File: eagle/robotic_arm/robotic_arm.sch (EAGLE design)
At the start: 104 parts, among them J2 (ID,OD)=(2.1,5.5)MM, SW1 5A/28V, Y1 16MHz

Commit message: Fucked up.  Forgot pull down and current limiting resistors on PWM driver to servosgit add -A  Added them.  Need to increase size of board and reroute
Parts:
- added R10, R12, R14, R4, R6, R8: 10KΩ, MrSwirlyEyes:RESISTORSMD-0805_1/8W_10K_5%
- added R11, R13, R15, R5, R7, R9: 100Ω, MrSwirlyEyes:RESISTORSMD-0805_1/8W_100_5%
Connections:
- new net N$1: R11.1, SERVO_WRIST.SIG
- new net N$4: R9.1, SERVO_THUMB.SIG
- new net N$6: R7.1, SERVO_INDEX.SIG
- new net N$7: R5.1, SERVO_MIDDLE.SIG
- new net N$8: R15.1, SERVO_RING.SIG
- new net N$9: R13.1, SERVO_PINKY.SIG
- net GND: now also R10.1, R12.1, R14.1, R4.1, R6.1, R8.1
- net SERVO_INDEX: now also R6.2, R7.2; no longer SERVO_MIDDLE.SIG
- net SERVO_MIDDLE: now also R4.2, R5.2; no longer SERVO_INDEX.SIG
- net SERVO_PINKY: now also R12.2, R13.2; no longer SERVO_WRIST.SIG
- net SERVO_RING: now also R14.2, R15.2; no longer SERVO_THUMB.SIG
- net SERVO_THUMB: now also R8.2, R9.2; no longer SERVO_RING.SIG
- net SERVO_WRIST: now also R10.2, R11.2; no longer SERVO_PINKY.SIG
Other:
- note removed: "WIRE DEMUX"
- moved on the sheet: C1, C10, C11, C12, C13, C14, C15, C16, C17, C2, C8, C9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

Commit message: Robotic Arm, Rev 1:  Completed all routes.  Messy as shit.  Much clean up to do
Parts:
- A6: value ANTENNASMD5 -> 2.4GHz/802.11/0.5dBi/3W
- B1: value 748421245 -> Impedence UNBAL/BAL (50Ω/100Ω)
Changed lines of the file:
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@@
 <setting verticaltext="up"/>
 </settings>
-<grid distance="0.1" unitdist="inch" unit="inch" style="lines" multiple="1" display="yes" altdistance="0.05" altunitdist="inch" altunit="inch"/>
+<grid distance="0.1" unitdist="inch" unit="inch" style="lines" multiple="1" display="no" altdistance="0.01" altunitdist="inch" altunit="inch"/>
 <layers>
 <layer number="1" name="Top" color="4" fill="1" visible="no" active="no"/>
@@
 <part name="R42" library="MrSwirlyEyes" deviceset="RESISTOR" device="SMD-0805_1/8W_10K_5%" value="10KΩ"/>
 <part name="C51" library="MrSwirlyEyes" deviceset="CAP_CERAMIC" device="_SMD-805_0.1UF-50V-10%" value="0.1uF/50V"/>
-<part name="MCU" library="MrSwirlyEyes" deviceset="ATMEGA128RFA1" device=""/>
+<part name="MCU" library="MrSwirlyEyes" deviceset="ATMEGA128RFA1" device="" value="ATMEGA128RFA1"/>
 <part name="C52" library="MrSwirlyEyes" deviceset="CAP_CERAMIC" device="_SMD-805_0.1UF-50V-10%" value="0.1uF/50V"/>
 <part name="C53" library="MrSwirlyEyes" deviceset="CAP_CERAMIC" device="_SMD-805-1UF-25V-10%" value="1uF/25V"/>
@@
 <part name="GND96" library="MrSwirlyEyes" deviceset="GND" device=""/>
 <part name="GND97" library="MrSwirlyEyes" deviceset="AGND" device=""/>
-<part name="B1" library="lib_kenmei" deviceset="BALUN" device="0805" value="748421245"/>
+<part name="B1" library="lib_kenmei" deviceset="BALUN" device="0805" value="Impedence UNBAL/BAL (50Ω/100Ω)"/>
 <part name="C61" library="MrSwirlyEyes" deviceset="CAP_CERAMIC" device="_SMD-805_22PF-250V-5%" value="22PF/250V"/>
 <part name="GND98" library="MrSwirlyEyes" deviceset="GND" device=""/>
 <part name="C62" library="MrSwirlyEyes" deviceset="CAP_CERAMIC" device="_SMD-805-0.75PF-100V-33%" value="0.75PF/100V"/>
 <part name="GND99" library="MrSwirlyEyes" deviceset="GND" device=""/>
-<part name="A6" library="lib_kenmei" deviceset="ANTENNA" device="SMD5"/>
+<part name="A6" library="lib_kenmei" deviceset="ANTENNA" device="SMD5" value="2.4GHz/802.11/0.5dBi/3W"/>
 <part name="R43" library="MrSwirlyEyes" deviceset="RESISTOR" device="SMD-0805_1/8W_10K_5%" value="10KΩ"/>
 <part name="SUPPLY71" library="MrSwirlyEyes" deviceset="VCC" device=""/>

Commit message: Rev 1: Board complete.  Sent to Fab
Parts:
- removed C56: 0.1uF/50V, MrSwirlyEyes:CAP_CERAMIC_SMD-805_0.1UF-50V-10%
- removed C84: 100UF/16V, MrSwirlyEyes:CAP_POLARIZED_ALUM-ELECTROLYTIC_SMD_100UF-16V-20%
- removed J2: (ID,OD)=(2.1,5.5)MM, MrSwirlyEyes:POWER_JACK-BARREL_ID2.1MM-OD5.5MM
- removed SUPPLY51, SUPPLY52: 2PT_GND_TIE, SparkFun-PowerSymbols:2PT_GND_TIE
- added ANALOG_BR, NOISE_BR: 2PT_GND_TIE, PiB_power_symbols:2PT_GND_TIE
- added C21, C23, C24: 1uF/25V, PiB_capacitors:1UF_SMD-805_25V-10%
- added C22: 0.1uF/50V, PiB_capacitors:0.1UF_SMD-805_50V-10%
- added J1: (ID,OD)=(2.1,5.5)MM, PiB_connectors:POWER_JACK-BARREL_ID2.1MM-OD5.5MM
- A6: device lib_kenmei:ANTENNASMD5 -> PiB_radio_frequency:ANTENNA_SMD-CHIP_2.4GHZ-0.5DBI-3W
- AVR_ISP: device MrSwirlyEyes:AVR_SPI_PRG_6NS -> PiB_connectors:AVR_SPI_PRG_6NS
- B1: device lib_kenmei:BALUN0805 -> PiB_radio_frequency:BALUN_SMD-0805_UNBAL/BAL-50/100
- BATT1: device MrSwirlyEyes:BATTERYPTH_HOLES -> PiB:BATTERYPTH_HOLES
- C1, C10, C12, C14, C16, C19, C26, C3, C4, C47, C48, C49, C5, C50, C51, C52, C54, C6, C63, C7, C79, C8, C81, C83, C93, C96, C98: device MrSwirlyEyes:CAP_CERAMIC_SMD-805_0.1UF-50V-10% -> PiB_capacitors:0.1UF_SMD-805_50V-10%
- C11, C13, C15, C17, C2, C9: value 100UF/16V -> 10uF/20V; device MrSwirlyEyes:CAP_POLARIZED_ALUM-ELECTROLYTIC_SMD_100UF-16V-20% -> PiB_capacitors:10UF-POLARIZED_SMD-1206_20V-20%
- C18, C25, C82, C92, C94, C95, C97: device MrSwirlyEyes:CAP_CERAMIC_SMD-805_10UF-25V-10% -> PiB_capacitors:10UF_CER_SMD-805_25V-10%
- C20: value 220uF/16V -> 100UF/16V; device MrSwirlyEyes:CAP_POLARIZED_ALUM-ELECTROLYTIC_SMD_220UF-16V-20% -> PiB_capacitors:100UF-POLARIZED_SMD_16V-20%
- C53, C55, C57, C58: device MrSwirlyEyes:CAP_CERAMIC_SMD-805-1UF-25V-10% -> PiB_capacitors:1UF_SMD-805_25V-10%
- C59, C60: device MrSwirlyEyes:CAP_CERAMIC_SMD-805_12PF-250V-5% -> PiB_capacitors:12PF_SMD-805_250V-5%
- C61: device MrSwirlyEyes:CAP_CERAMIC_SMD-805_22PF-250V-5% -> PiB_capacitors:22PF_SMD-805_250V-5%
- C62: device MrSwirlyEyes:CAP_CERAMIC_SMD-805-0.75PF-100V-33% -> PiB_capacitors:0.75PF_SMD-805_100V-33%
- C80: device MrSwirlyEyes:CAP_POLARIZED_ALUM-ELECTROLYTIC_SMD_220UF-16V-20% -> PiB_capacitors:220UF-POLARIZED_SMD_16V-20%
- C85: value 1uF/25V -> 0.1uF/50V; device MrSwirlyEyes:CAP_CERAMIC_SMD-805-1UF-25V-10% -> PiB_capacitors:0.1UF_SMD-805_50V-10%
- D1, D6, D7: device MrSwirlyEyes:DIODE_GEN-PURPSMD_GP_1A-50V-SOD123F -> PiB_discrete_semiconductors:DIODE_GENERAL-PURPOSE_SMD_GP_1A-50V
- DEMUX1: device MrSwirlyEyes:CD74HC4067-SM96_16:1_MUX-DEMUX -> PiB:CD74HC4067-SM96_16:1_MUX-DEMUX
- FSR_INDEX, FSR_MIDDLE, FSR_PINKY, FSR_RING, FSR_THUMB: device MrSwirlyEyes:FSR_FORCE-SENSATIVE-RESISTOR_PRESS-SENSOR -> PiB:FSR_FORCE-SENSATIVE-RESISTOR_PRESS-SENSOR
- JP1: device MrSwirlyEyes:FTDIPTH-RA -> PiB_connectors:FTDIPTH-RA
- L1, L2: device MrSwirlyEyes:INDUCTORSMD-805_10UH-0.5A-0.65OHM-10% -> PiB_inductors:10UH_SMD-805_0.5A-0.65OHM-10%
- L3: device MrSwirlyEyes:LED_SMD-805_DISCRETE_BLUE -> PiB_leds:LED_SMD-0805_DISCRETE_BLUE
- L4: device MrSwirlyEyes:LED_SMD-805_DISCRETE_GREEN -> PiB_leds:LED_SMD-0805_DISCRETE_GREEN
- L5: device MrSwirlyEyes:LED_SMD-805_DISCRETE_RED -> PiB_leds:LED_SMD-0805_DISCRETE_RED
- MCU: device MrSwirlyEyes:ATMEGA128RFA1 -> PiB_ic_microcontrollers:ATMEGA128RFA1_VFQFN-64_EXPOSED-PAD
- PWM_DRIVER: device MrSwirlyEyes:PCA9685_16-CH_12-BIT_PWM-DRIVER -> PiB:PCA9685_16-CH_12-BIT_PWM-DRIVER
- R1, R10, R12, R14, R16, R39, R4, R40, R41, R42, R43, R6, R8: device MrSwirlyEyes:RESISTORSMD-0805_1/8W_10K_5% -> PiB_resistors:10KΩ_SMD-0805_1/8W-5%
- R11, R13, R15, R5, R7, R9: device MrSwirlyEyes:RESISTORSMD-0805_1/8W_100_5% -> PiB_resistors:100Ω_SMD-0805_1/8W-5%
- R17, R18: device MrSwirlyEyes:RESISTORSMD-0805_1/8W_4.7K_5% -> PiB_resistors:4.7KΩ_SMD-0805_1/8W-5%
- R2: device MrSwirlyEyes:RESISTORSMD-0805_1/8W_2K_5% -> PiB_resistors:2KΩ_SMD-0805_1/8W-5%
- R3: device MrSwirlyEyes:RESISTORSMD-0805_1/8W_1K_5% -> PiB_resistors:1KΩ_SMD-0805_1/8W-5%
- S7: device MrSwirlyEyes:SWITCH_MOMENTARY_SPSTSPST-SMD-50MA-12V_L5.2-W5.2 -> PiB_switches:SWITCH_MOMENTARYSPST-SMD-50MA-12V_L5.2-W5.2
- SERVO_INDEX, SERVO_MIDDLE, SERVO_PINKY, SERVO_RING, SERVO_THUMB, SERVO_WRIST: device MrSwirlyEyes:SERVO-HK15298B -> PiB:SERVO-HK15298B
- SW1: device MrSwirlyEyes:SWITCH_SPDT5A-28V_13L-7W -> PiB_switches:SWITCH_SPDT_VERT_PTH_5A-28V_13L-7W
- TEMP_INDEX, TEMP_MIDDLE, TEMP_PINKY, TEMP_RING, TEMP_THUMB: device MrSwirlyEyes:TEMPERATURE-SENSOR_TMP36 -> PiB:TEMPERATURE-SENSOR_TMP36
- VREG1: device MrSwirlyEyes:VREG_MIC29501-5.0_LINEAR_ULDO_5A-5VMIC29501-5.0_5A-5V -> PiB_ic_power:VREG_MIC29501-5.0_LINEAR_ULDO_5A-5VMIC29501-5.0_5A-5V
- VREG3: device MrSwirlyEyes:VREG_TPS76833_ULDO_FAST-TRANSIENT_1A-3.3VTPS76833QDR_1A-3.3V -> PiB_ic_power:VREG_TPS76833_ULDO_FAST-TRANSIENT_1A-3.3VTPS76833QDR_1A-3.3V
- Y1: device MrSwirlyEyes:CRYSTAL_ABM3B_16MHZ_18PF -> PiB:CRYSTAL_ABM3B_16MHZ_18PF
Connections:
- new net N$10: C21.1, MCU.DVDD
- new net N$11: C57.1, MCU.AVDD
- net 5V: now also C20.A
- net A0: no longer DEMUX1.SIG
- net A5: now also DEMUX1.SIG
- net AGND: now also ANALOG_BR.P$2, C22.2, C23.2, C24.2; no longer SUPPLY52.P$2
- net AVCC: now also C22.1, C23.1, C24.1; no longer C56.1, C57.1, MCU.AVDD
- net BATT_+: now also J1.PWR, SW1.2; no longer J2.PWR, SW1.P
- net BATT_-: now also J1.GND@1; no longer J2.GND@1
- net FSR_INDEX: now also FSR_RING.-, R39.2; no longer FSR_INDEX.-, R41.2
- net FSR_PINKY: now also FSR_THUMB.-, R42.2; no longer FSR_PINKY.-, R16.2
- net FSR_RING: now also FSR_INDEX.-, R41.2; no longer FSR_RING.-, R39.2
- net FSR_THUMB: now also FSR_PINKY.-, R16.2; no longer FSR_THUMB.-, R42.2
- net GND: now also C21.2, J1.GND@2, NOISE_BR.P$2; no longer C20.K, C56.2, C84.K, J2.GND@2, SUPPLY51.P$2
- net N$38: now also ANALOG_BR.P$1; no longer SUPPLY52.P$1
- net NGND: now also C20.K, NOISE_BR.P$1; no longer SUPPLY51.P$1
- net VBATT: now also SW1.1; no longer C20.A, C84.A, SW1.S1
- net VCC: no longer MCU.DVDD
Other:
- moved on the sheet: C20, C52, C53, C54, C55, C57, C58, C63, C85

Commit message: Modified code to work with new PCB board.  Removed libraries, placed in new repo.  Finished and printed Robotic Arm PCB board.  Tested and WORKS!  Started on Touch Glove PCB
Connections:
- net A0: now also MCU.(ADC0/A0*)PF0; no longer MCU.PF0(ADC0)
- net A1: now also MCU.(ADC1/A1*)PF1; no longer MCU.PF1(ADC1)
- net A2: now also MCU.(ADC2/DIG2/A2*)PF2; no longer MCU.PF2(ADC2/DIG2)
- net A3: now also MCU.(ADC3/DIG4/A3*)PF3; no longer MCU.PF3(ADC3/DIG4)
- net A4: now also MCU.(ADC4/TCK/A4*)PF4; no longer MCU.PF4(ADC4/TCK)
- net A5: now also MCU.(ADC5/TMS/A5*)PF5; no longer MCU.PF5(ADC5/TMS)
- net A6: now also MCU.(ADC6/TDO/A6*)PF6; no longer MCU.PF6(ADC6/TDO)
- net A7: now also MCU.(ADC7/TDI/A7*)PF7; no longer MCU.PF7(ADC7/TDI)
- net MISO: now also MCU.(PDO/PCINT3/MISO/D12)PB3; no longer MCU.PB3(MISO/PDO/PCINT3)
- net MOSI: now also MCU.(PDI/PCINT2/MOSI/D11)PB2; no longer MCU.PB2(MOSI/PDI/PCINT2)
- net PB4: now also MCU.(PCINT4/OC2A/D9-PWM9)PB4; no longer MCU.PB4(OC2A/PCINT4)
- net PB5: now also MCU.(PCINT5/OC1A/D8-PWM8)PB5; no longer MCU.PB5(OC1A/PCINT5)
- net PB6: now also MCU.(PCINT6/OC1B/D34-PWM34)PB6; no longer MCU.PB6(OC1B/PCINT6)
- net PB7: now also MCU.(PCINT7/OC0A/OC1C/D35-PWM35)PB7; no longer MCU.PB7(OC0A/OC1C/PCINT7)
- net PD4: now also MCU.(ICP1/D22)PD4; no longer MCU.PD4(ICP1)
- net PD5: now also MCU.(XCK1/D23)PD5; no longer MCU.PD5(XCK1)
- net PD6: now also MCU.(T1/D24)PD6; no longer MCU.PD6(T1)
- net PD7: now also MCU.(T0/D25)PD7; no longer MCU.PD7(T0)
- net PE2: now also MCU.(XCK0/AIN0/D2)PE2; no longer MCU.PE2(XCK0/AIN0)
- net PE3: now also MCU.(AIN1/OC3A/D3-PWM3)PE3; no longer MCU.PE3(OC3A/AIN1)
- net PE4: now also MCU.(INT4/OC3B/D4-PWM4)PE4; no longer MCU.PE4(OC3B/INT4)
- net PE5: now also MCU.(INT5/OC3C/D5-PWM5)PE5; no longer MCU.PE5(OC3C/INT5)
- net PE6: now also MCU.(T3/INT6/D6)PE6; no longer MCU.PE6(T3/INT6)
- net PE7: now also MCU.(ICP3/INT7/CLKO/D7)PE7; no longer MCU.PE7(ICP3/INT7/CLKO)
- net PG0: now also MCU.(DIG3/D16)PG0; no longer MCU.PG0(DIG3)
- net PG1: now also MCU.(DIG1/D17)PG1; no longer MCU.PG1(DIG1)
- net PG2: now also MCU.(AMR/D18)PG2; no longer MCU.PG2(AMR)
- net PG3: now also MCU.(TOSC2)PG3; no longer MCU.PG3(TOSC2)
- net PG4: now also MCU.(TOSC1)PG4; no longer MCU.PG4(TOSC1)
- net PG5: now also MCU.(OC0B/D19-PWM19)PG5; no longer MCU.PG5(OC0B)
- net RX0: now also MCU.(PCINT8/RXD0/D0)PE0; no longer MCU.PE0(RXD0/PCINT8)
- net RX1: now also MCU.(INT2/RXD1/D20)PD2; no longer MCU.PD2(RXD1/INT2)
- net SCK: now also MCU.(PCINT1/SCK/D13)PB1; no longer MCU.PB1(SCK/PCINT1)
- net SCL: now also MCU.(INT0/SCL/D15)PD0; no longer MCU.PD0(SCL/INT0)
- net SDA: now also MCU.(INT1/SDA/D14)PD1; no longer MCU.PD1(SDA/INT1)
- net SSN: now also MCU.(PCINT0/SSN/D10)PB0; no longer MCU.PB0(SSN/PCINT0)
- net TX0: now also MCU.(TXD0/D1)PE1; no longer MCU.PE1(TXD0)
- net TX1: now also MCU.(INT3/TXD1/D21)PD3; no longer MCU.PD3(TXD1/INT3)

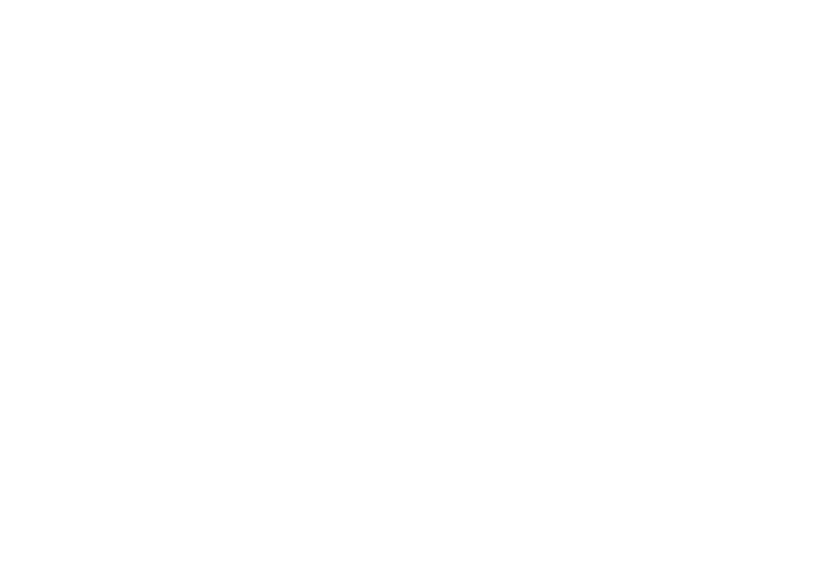
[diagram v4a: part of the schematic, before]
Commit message: Rev 2: Fixed the one baby mistake I found from a via not being connected to GND on the exposed pad under the ATMEGA128RFA1
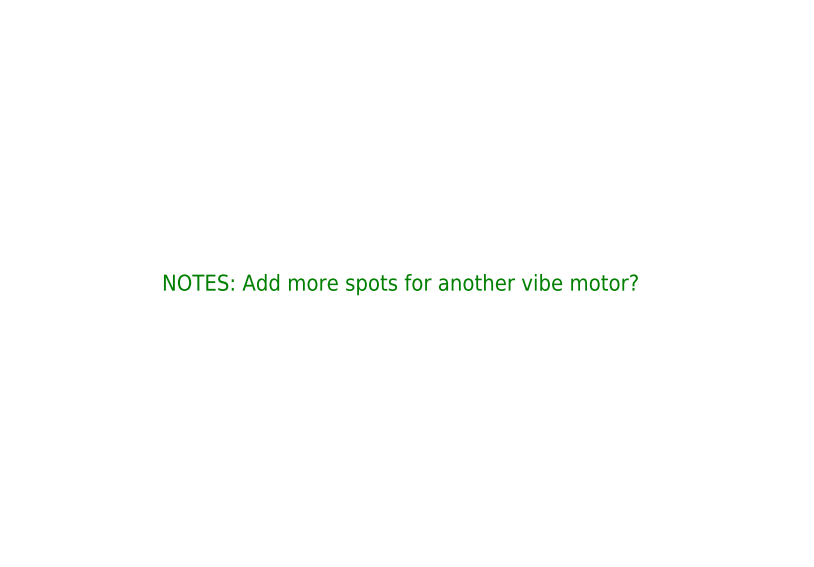
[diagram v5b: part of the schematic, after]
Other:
- note added: "NOTES: Add more spots for another vibe motor?"
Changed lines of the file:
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@@
 <text x="279.4" y="271.78" size="1.778" layer="97">D7 --&gt; S2 of DEMUX</text>
 <text x="279.4" y="335.28" size="1.778" layer="97">D10 --&gt; S3 of DEMUX</text>
+<text x="492.76" y="368.3" size="1.778" layer="91">NOTES: Add more spots for another vibe motor?</text>
 </plain>
 <instances>
